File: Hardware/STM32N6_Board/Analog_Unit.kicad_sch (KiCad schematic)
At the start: 16 parts, among them SW2 SW_Push, U1 STM32N657I0H3Q, U10 STMPS2151STR, U12 ECMF2-40A100N6, U13 ECMF2-40A100N6, U14 ECMF2-40A100N6, U9 ECMF2-40A100N6

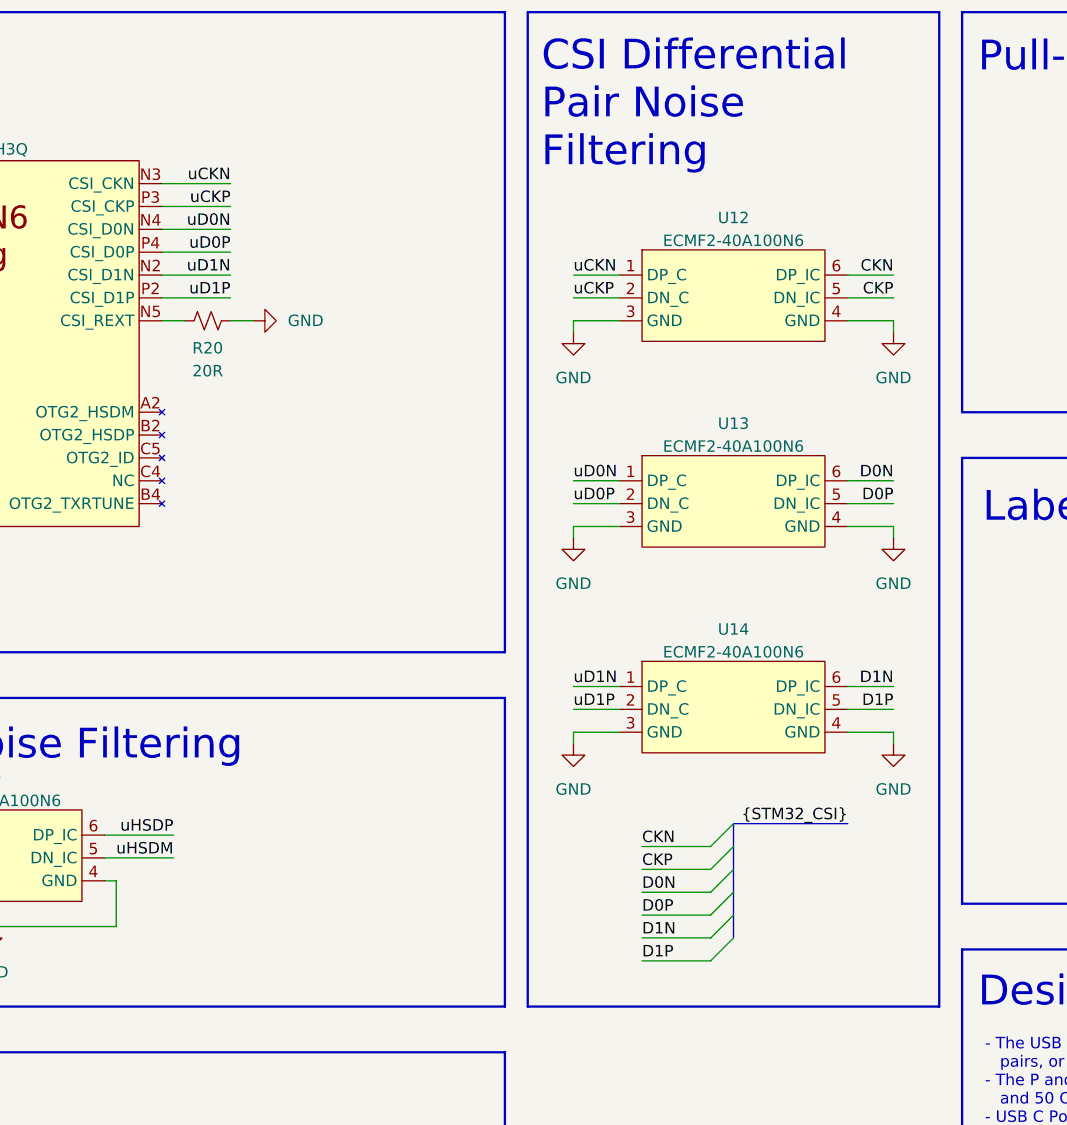
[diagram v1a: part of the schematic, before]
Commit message: added decoupling caps and other stuffs
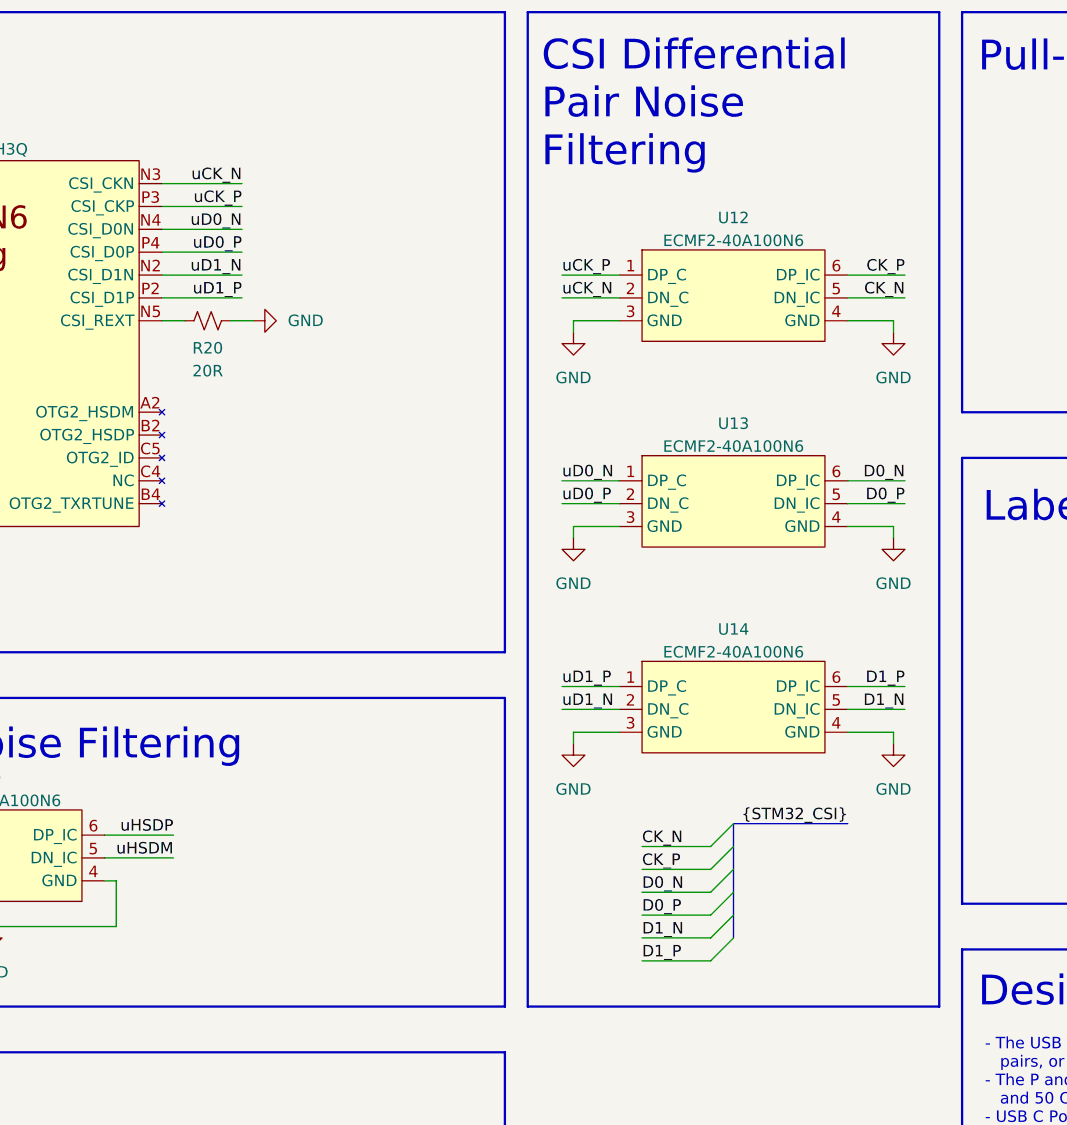
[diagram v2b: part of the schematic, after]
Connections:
- net CKN renamed CK_P
- net CKP renamed CK_N
- net D0N renamed D0_N
- net D0P renamed D0_P
- net D1N renamed D1_P
- net D1P renamed D1_N
- net uCKN renamed uCK_N
- net uCK_N: now also U12.2 (DN_C); no longer U12.1 (DP_C)
- net uCKP renamed uCK_P
- net uCK_P: now also U12.1 (DP_C); no longer U12.2 (DN_C)
- net uD0N renamed uD0_N
- net uD0P renamed uD0_P
- net uD1N renamed uD1_N
- net uD1_N: now also U14.2 (DN_C); no longer U14.1 (DP_C)
- net uD1P renamed uD1_P
- net uD1_P: now also U14.1 (DP_C); no longer U14.2 (DN_C)
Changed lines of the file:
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@@
 	)
 	(bus_alias "STM32_CSI"
-		(members "CKN" "CKP" "D0N" "D0P" "D1N" "D1P" "EN")
+		(members "CK_N" "CK_P" "D0_N" "D0_P" "D1_N" "D1_P" "EN")
 	)
 	(bus_alias "STM32_USB"
@@
 	(wire
 		(pts
-			(xy 88.9 40.64) (xy 96.52 40.64)
+			(xy 88.9 40.64) (xy 97.79 40.64)
 		)
 		(stroke
@@
 	(wire
 		(pts
-			(xy 134.62 45.72) (xy 139.7 45.72)
-		)
-		(stroke
-			(width 0)
-			(type default)
-		)
-	)
-	(wire
-		(pts
 			(xy 49.53 107.95) (xy 57.15 107.95)
 		)
@@
 	(wire
 		(pts
-			(xy 134.62 93.98) (xy 139.7 93.98)
-		)
-		(stroke
-			(width 0)
-			(type default)
-		)
-	)
-	(wire
-		(pts
 			(xy 243.84 33.02) (xy 252.73 33.02)
 		)
@@
 	(wire
 		(pts
-			(xy 88.9 38.1) (xy 96.52 38.1)
+			(xy 88.9 38.1) (xy 97.79 38.1)
 		)
 		(stroke
@@
 	(wire
 		(pts
-			(xy 165.1 91.44) (xy 170.18 91.44)
-		)
-		(stroke
-			(width 0)
-			(type default)
-		)
-	)
-	(wire
-		(pts
-			(xy 134.62 68.58) (xy 139.7 68.58)
+			(xy 165.1 91.44) (xy 171.45 91.44)
 		)
 		(stroke
@@
 	(wire
 		(pts
-			(xy 165.1 45.72) (xy 170.18 45.72)
+			(xy 165.1 45.72) (xy 171.45 45.72)
 		)
 		(stroke
@@
 	(wire
 		(pts
-			(xy 165.1 68.58) (xy 170.18 68.58)
+			(xy 165.1 68.58) (xy 171.45 68.58)
 		)
 		(stroke
@@
 	(wire
 		(pts
-			(xy 165.1 71.12) (xy 170.18 71.12)
+			(xy 165.1 71.12) (xy 171.45 71.12)
 		)
 		(stroke
@@
 		)
 	)
+	(wire
+		(pts
+			(xy 133.35 48.26) (xy 139.7 48.26)
+		)
+		(stroke
+			(width 0)
+			(type default)
+		)
+	)
+	(wire
+		(pts
+			(xy 133.35 71.12) (xy 139.7 71.12)
+		)
+		(stroke
+			(width 0)
+			(type default)
+		)
+	)
 	(bus
 		(pts
@@
 	(wire
 		(pts
+			(xy 133.35 68.58) (xy 139.7 68.58)
+		)
+		(stroke
+			(width 0)
+			(type default)
+		)
+	)
+	(wire
+		(pts
 			(xy 220.98 31.75) (xy 220.98 40.64)
 		)
@@
 	(wire
 		(pts
-			(xy 134.62 71.12) (xy 139.7 71.12)
+			(xy 133.35 45.72) (xy 139.7 45.72)
 		)
 		(stroke
@@
 	(wire
 		(pts
-			(xy 88.9 48.26) (xy 96.52 48.26)
+			(xy 88.9 48.26) (xy 97.79 48.26)
 		)
 		(stroke
@@
 	(wire
 		(pts
-			(xy 165.1 93.98) (xy 170.18 93.98)
+			(xy 165.1 93.98) (xy 171.45 93.98)
+		)
+		(stroke
+			(width 0)
+			(type default)
+		)
+	)
+	(wire
+		(pts
+			(xy 133.35 93.98) (xy 139.7 93.98)
 		)
 		(stroke
@@
 	(wire
 		(pts
-			(xy 88.9 43.18) (xy 96.52 43.18)
+			(xy 88.9 43.18) (xy 97.79 43.18)
 		)
 		(stroke
@@
 	(wire
 		(pts
-			(xy 134.62 48.26) (xy 139.7 48.26)
-		)
-		(stroke
-			(width 0)
-			(type default)
-		)
-	)
-	(wire
-		(pts
 			(xy 69.85 118.11) (xy 55.88 118.11)
 		)
@@
 	(wire
 		(pts
-			(xy 165.1 48.26) (xy 170.18 48.26)
+			(xy 165.1 48.26) (xy 171.45 48.26)
 		)
 		(stroke
@@
 	(wire
 		(pts
-			(xy 88.9 45.72) (xy 96.52 45.72)
+			(xy 88.9 45.72) (xy 97.79 45.72)
 		)
 		(stroke
@@
 	(wire
 		(pts
+			(xy 133.35 91.44) (xy 139.7 91.44)
+		)
+		(stroke
+			(width 0)
+			(type default)
+		)
+	)
+	(wire
+		(pts
 			(xy 209.55 33.02) (xy 209.55 31.75)
 		)
@@
 	(wire
 		(pts
-			(xy 88.9 35.56) (xy 96.52 35.56)
+			(xy 88.9 35.56) (xy 97.79 35.56)
 		)
 		(stroke
@@
 		(pts
 			(xy 134.62 96.52) (xy 139.7 96.52)
-		)
-		(stroke
-			(width 0)
-			(type default)
-		)
-	)
-	(wire
-		(pts
-			(xy 134.62 91.44) (xy 139.7 91.44)
 		)
 		(stroke
@@
 		)
 	)
-	(label "CKP"
-		(at 170.18 48.26 180)
+	(label "CK_P"
+		(at 171.45 45.72 180)
 		(effects
 			(font
@@
 		)
 	)
-	(label "D1N"
+	(label "D1_N"
 		(at 142.24 119.38 0)
 		(effects
@@
 		)
 	)
-	(label "D1P"
+	(label "D1_P"
 		(at 142.24 121.92 0)
 		(effects
@@
 		)
 	)
-	(label "uCKP"
-		(at 134.62 48.26 0)
+	(label "uCK_P"
+		(at 133.35 45.72 0)
 		(effects
 			(font
@@
 		)
 	)
-	(label "uD1N"
-		(at 96.52 45.72 180)
+	(label "uD1_N"
+		(at 97.79 45.72 180)
 		(effects
 			(font
@@
 		)
 	)
-	(label "D0P"
+	(label "D0_P"
 		(at 142.24 116.84 0)
 		(effects
@@
 		)
 	)
-	(label "uD1P"
-		(at 134.62 93.98 0)
-		(effects
-			(font
-				(size 1.27 1.27)
-			)
-			(justify left bottom)
-		)
-	)
-	(label "uCKP"
-		(at 96.52 38.1 180)
+	(label "uD1_P"
+		(at 133.35 91.44 0)
+		(effects
+			(font
+				(size 1.27 1.27)
+			)
+			(justify left bottom)
+		)
+	)
+	(label "uCK_P"
+		(at 97.79 38.1 180)
 		(effects
 			(font
@@
 		)
 	)
-	(label "D0P"
-		(at 170.18 71.12 180)
+	(label "D0_P"
+		(at 171.45 71.12 180)
 		(effects
 			(font
@@
 		)
 	)
-	(label "CKP"
+	(label "CK_P"
 		(at 142.24 111.76 0)
 		(effects
@@
 		)
 	)
-	(label "D0N"
-		(at 170.18 68.58 180)
+	(label "D0_N"
+		(at 171.45 68.58 180)
 		(effects
 			(font
@@
 		)
 	)
-	(label "CKN"
+	(label "CK_N"
 		(at 142.24 109.22 0)
 		(effects
@@
 		)
 	)
-	(label "uD0N"
-		(at 96.52 40.64 180)
+	(label "uD0_N"
+		(at 97.79 40.64 180)
 		(effects
 			(font
@@
 		)
 	)
-	(label "uD0P"
-		(at 96.52 43.18 180)
+	(label "uD0_P"
+		(at 97.79 43.18 180)
 		(effects
 			(font
@@
 		)
 	)
-	(label "uD0P"
-		(at 134.62 71.12 0)
-		(effects
-			(font
-				(size 1.27 1.27)
-			)
-			(justify left bottom)
-		)
-	)
-	(label "CKN"
-		(at 170.18 45.72 180)
+	(label "uD0_P"
+		(at 133.35 71.12 0)
+		(effects
+			(font
+				(size 1.27 1.27)
+			)
+			(justify left bottom)
+		)
+	)
+	(label "CK_N"
+		(at 171.45 48.26 180)
 		(effects
 			(font
@@
 		)
 	)
-	(label "uD1N"
-		(at 134.62 91.44 0)
+	(label "uD1_N"
+		(at 133.35 93.98 0)
 		(effects
 			(font
@@
 		)
 	)
-	(label "D1P"
-		(at 170.18 93.98 180)
+	(label "D1_P"
+		(at 171.45 91.44 180)
 		(effects
 			(font
@@
 		)
 	)
-	(label "uCKN"
-		(at 96.52 35.56 180)
+	(label "uCK_N"
+		(at 97.79 35.56 180)
 		(effects
 			(font
@@
 		)
 	)
-	(label "D1N"
-		(at 170.18 91.44 180)
+	(label "D1_N"
+		(at 171.45 93.98 180)
 		(effects
 			(font
@@
 		)
 	)
-	(label "D0N"
+	(label "D0_N"
 		(at 142.24 114.3 0)
 		(effects
@@
 		)
 	)
-	(label "uD1P"
-		(at 96.52 48.26 180)
+	(label "uD1_P"
+		(at 97.79 48.26 180)
 		(effects
 			(font
@@
 		)
 	)
-	(label "uD0N"
-		(at 134.62 68.58 0)
+	(label "uD0_N"
+		(at 133.35 68.58 0)
 		(effects
 			(font
@@
 		)
 	)
-	(label "uCKN"
-		(at 134.62 45.72 0)
-		(effects
-			(font
+	(label "uCK_N"
+		(at 133.35 48.26 0)
+		(effects
+			(font

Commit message: almost finished with the board
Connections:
- net EN renamed EN_USB
- net HSDM renamed HSD_P
- net HSDP renamed HSD_N
- net uHSDM renamed uHSD_N
- net uHSD_N: now also U9.6 (DP_IC); no longer U9.5 (DN_IC)
- net uHSDP renamed uHSD_P
- net uHSD_P: now also U9.5 (DN_IC); no longer U9.6 (DP_IC)
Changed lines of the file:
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@@
 	)
 	(bus_alias "STM32_USB"
-		(members "CC1" "CC2" "HSDP" "HSDM" "FAULT" "EN_USB" "VBUS")
+		(members "CC1" "CC2" "HSD_P" "HSD_N" "FAULT" "EN_USB" "VBUS")
 	)
 	(rectangle
@@
 		)
 	)
-	(label "HSDM"
-		(at 49.53 110.49 0)
+	(label "HSD_N"
+		(at 49.53 107.95 0)
 		(effects
 			(font
@@
 		)
 	)
-	(label "uHSDP"
-		(at 90.17 107.95 180)
+	(label "uHSD_P"
+		(at 90.17 110.49 180)
 		(effects
 			(font
@@
 		)
 	)
-	(label "EN"
+	(label "EN_USB"
 		(at 48.26 163.83 0)
 		(effects
@@
 		)
 	)
-	(label "uHSDM"
-		(at 90.17 110.49 180)
+	(label "uHSD_N"
+		(at 90.17 107.95 180)
 		(effects
 			(font
@@
 		)
 	)
-	(label "uHSDP"
+	(label "uHSD_P"
 		(at 33.02 43.18 0)
 		(effects
@@
 		)
 	)
-	(label "HSDP"
-		(at 49.53 107.95 0)
+	(label "HSD_P"
+		(at 49.53 110.49 0)
 		(effects
 			(font
@@
 		)
 	)
-	(label "uHSDM"
+	(label "uHSD_N"
 		(at 33.02 45.72 0)
 		(effects

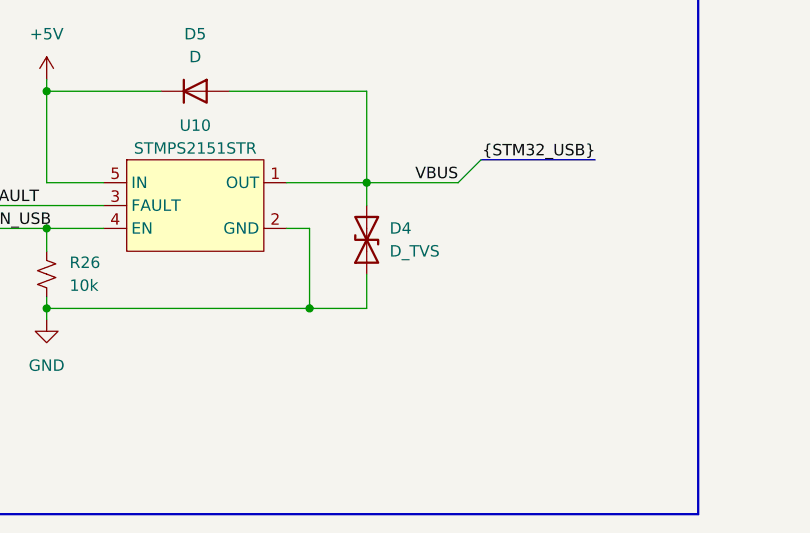
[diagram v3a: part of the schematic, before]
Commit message: Added the gerbers, drill files, BOM, and CPL files
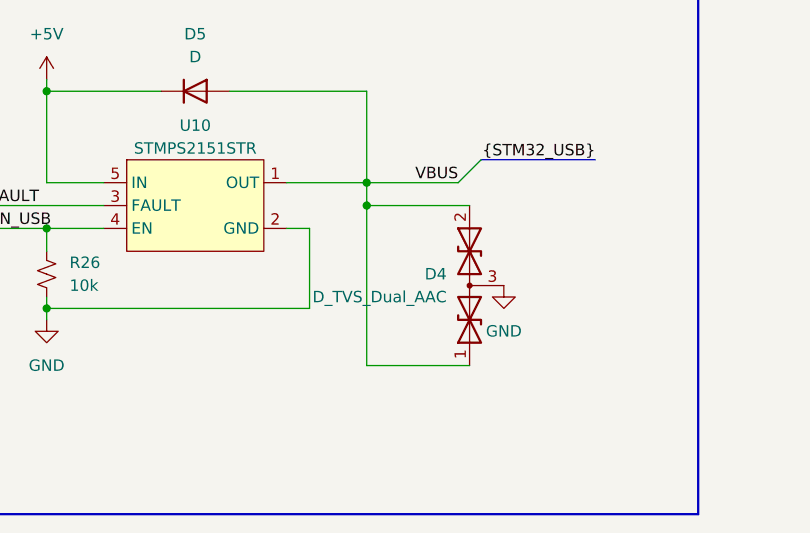
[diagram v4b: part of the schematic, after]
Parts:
- removed D4: D_TVS, LED_SMD:LED_0805_2012Metric_Pad1.15x1.40mm_HandSolder, symbol Device:D_TVS
- added D4: D_TVS_Dual_AAC, Package_TO_SOT_SMD:SOT-723, symbol Device:D_TVS_Dual_AAC
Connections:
- net GND: now also D4.3 (common)
- net VBUS: now also D4.1 (A1), D4.2 (A2)
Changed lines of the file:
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@@
 	)
 	(junction
-		(at 83.82 172.72)
+		(at 90.17 161.29)
 		(diameter 0)
 		(color 0 0 0 0)
@@
 	(wire
 		(pts
+			(xy 90.17 158.75) (xy 90.17 161.29)
+		)
+		(stroke
+			(width 0)
+			(type default)
+		)
+	)
+	(wire
+		(pts
 			(xy 205.74 40.64) (xy 210.82 40.64)
 		)
@@
 	(wire
 		(pts
-			(xy 90.17 168.91) (xy 90.17 172.72)
-		)
-		(stroke
-			(width 0)
-			(type default)
-		)
-	)
-	(wire
-		(pts
 			(xy 196.85 40.64) (xy 204.47 40.64)
 		)
@@
 	(wire
 		(pts
-			(xy 90.17 172.72) (xy 83.82 172.72)
-		)
-		(stroke
-			(width 0)
-			(type default)
-		)
-	)
-	(wire
-		(pts
 			(xy 165.1 68.58) (xy 171.45 68.58)
 		)
@@
 		)
 	)
-	(wire
-		(pts
-			(xy 90.17 158.75) (xy 90.17 161.29)
-		)
-		(stroke
-			(width 0)
-			(type default)
-		)
-	)
 	(bus
 		(pts
@@
 		)
 	)
+	(wire
+		(pts
+			(xy 90.17 161.29) (xy 101.6 161.29)
+		)
+		(stroke
+			(width 0)
+			(type default)
+		)
+	)
 	(bus
 		(pts
@@
 	(wire
 		(pts
+			(xy 101.6 179.07) (xy 90.17 179.07)
+		)
+		(stroke
+			(width 0)
+			(type default)
+		)
+	)
+	(wire
+		(pts
 			(xy 205.74 50.8) (xy 220.98 50.8)
 		)
@@
 	(wire
 		(pts
+			(xy 90.17 161.29) (xy 90.17 179.07)
+		)
+		(stroke
+			(width 0)
+			(type default)
+		)
+	)
+	(wire
+		(pts
 			(xy 33.02 66.04) (xy 43.18 66.04)
 		)
@@
 	)
 	(symbol
+		(lib_id "Device:D_TVS_Dual_AAC")
+		(at 101.6 170.18 90)
+		(unit 1)
+		(exclude_from_sim no)
+		(in_bom yes)
+		(on_board yes)
+		(dnp no)
+		(fields_autoplaced yes)
+		(property "Reference" "D4"
+			(at 99.06 168.9099 90)
+			(effects
+				(font
+					(size 1.27 1.27)
+				)
+				(justify left)
+			)
+		)
+		(property "Value" "D_TVS_Dual_AAC"
+			(at 99.06 171.4499 90)
+			(effects
+				(font
+					(size 1.27 1.27)
+				)
+				(justify left)
+			)
+		)
+		(property "Footprint" "Package_TO_SOT_SMD:SOT-723"
+			(at 101.6 173.99 0)
+			(effects
+				(font
+					(size 1.27 1.27)
+				)
+				(hide yes)
+			)
+		)
+		(property "Datasheet" "~"
+			(at 101.6 173.99 0)
+			(effects
+				(font
+					(size 1.27 1.27)
+				)
+				(hide yes)
+			)
+		)
+		(property "Description" "Bidirectional dual transient-voltage-suppression diode, center on pin 3"
+			(at 101.6 170.18 0)
+			(effects
+				(font
+					(size 1.27 1.27)
+				)
+				(hide yes)
+			)
+		)
+		(pin "3"
+		)
+		(pin "1"
+		)
+		(pin "2"
+		)
+		(instances
+			(project ""
+				(path "/4869b3db-9bd3-4900-9c3c-205f01100fa6/892c9571-9add-4117-8957-9fe1c7a06a87"
+					(reference "D4")
+					(unit 1)
+				)
+			)
+		)
+	)
+	(symbol
 		(lib_name "R_Small_US_1")
 		(lib_id "Device:R_Small_US")
@@
 	)
 	(symbol
-		(lib_id "Device:D_TVS")
-		(at 90.17 165.1 90)
-		(unit 1)
-		(exclude_from_sim no)
-		(in_bom yes)
-		(on_board yes)
-		(dnp no)
-		(fields_autoplaced yes)
-		(property "Reference" "D4"
-			(at 92.71 163.8299 90)
-			(effects
-				(font
-					(size 1.27 1.27)
-				)
-				(justify right)
-			)
-		)
-		(property "Value" "D_TVS"
-			(at 92.71 166.3699 90)
-			(effects
-				(font
-					(size 1.27 1.27)
-				)
-				(justify right)
-			)
-		)
-		(property "Footprint" "LED_SMD:LED_0805_2012Metric_Pad1.15x1.40mm_HandSolder"
-			(at 90.17 165.1 0)
-			(effects
-				(font
-					(size 1.27 1.27)
-				)
-				(hide yes)
-			)
-		)
-		(property "Datasheet" "~"
-			(at 90.17 165.1 0)
-			(effects
-				(font
-					(size 1.27 1.27)
-				)
-				(hide yes)
-			)
-		)
-		(property "Description" "Bidirectional transient-voltage-suppression diode"
-			(at 90.17 165.1 0)
-			(effects
-				(font
-					(size 1.27 1.27)
-				)
-				(hide yes)
-			)
-		)
-		(pin "1"
-		)
-		(pin "2"
-		)
-		(instances
-			(project ""
-				(path "/4869b3db-9bd3-4900-9c3c-205f01100fa6/892c9571-9add-4117-8957-9fe1c7a06a87"
-					(reference "D4")
-					(unit 1)
-				)
-			)
-		)
-	)
-	(symbol
 		(lib_id "power:GND")
 		(at 170.18 74.93 0)
@@
 					(unit 1)
 				)
+			)
+		)
+	)
+	(symbol
+		(lib_id "power:GND")
+		(at 105.41 170.18 0)
+		(unit 1)
+		(exclude_from_sim no)
+		(in_bom yes)
+		(on_board yes)
+		(dnp no)
+		(fields_autoplaced yes)
+		(property "Reference" "#PWR05"
+			(at 105.41 176.53 0)
+			(effects
+				(font
+					(size 1.27 1.27)
+				)
+				(hide yes)
+			)
+		)
+		(property "Value" "GND"
+			(at 105.41 175.26 0)
+			(effects
+				(font
+					(size 1.27 1.27)
+				)
+			)
+		)
+		(property "Footprint" ""
+			(at 105.41 170.18 0)
+			(effects
+				(font
+					(size 1.27 1.27)
+				)
+				(hide yes)
+			)
+		)
+		(property "Datasheet" ""
+			(at 105.41 170.18 0)
+			(effects
+				(font
+					(size 1.27 1.27)
+				)
+				(hide yes)
+			)
+		)
+		(property "Description" "Power symbol creates a global label with name \"GND\" , ground"
+			(at 105.41 170.18 0)
+			(effects
+				(font
+					(size 1.27 1.27)
+				)
+				(hide yes)
+			)
+		)
+		(pin "1"
+		)
+		(instances
+			(project "STM32N6_Board"
+				(path "/4869b3db-9bd3-4900-9c3c-205f01100fa6/892c9571-9add-4117-8957-9fe1c7a06a87"
+					(reference "#PWR05")
+					(unit 1)
+				)
